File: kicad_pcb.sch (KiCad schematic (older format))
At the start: 162 parts, among them J1 USB_B_Mini, SW1 SW_Push, U1 ATmega32U4-AU, Y1 16Mhz

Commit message: further tracing applied
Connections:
- net COL0: now also U1.29 (PB5)
- net COL1: now also U1.30 (PB6)
- net COL10: now also U1.22 (PD5)
- net COL11: now also U1.21 (PD3)
- net COL12: now also U1.20 (PD2)
- net COL13: now also U1.19 (PD1)
- net COL14: now also U1.12 (PB7)
- net COL2: now also U1.41 (PF0)
- net COL3: now also U1.31 (PC6)
- net COL4: now also U1.32 (PC7)
- net COL5: now also U1.18 (PD0)
- net COL6: now also U1.1 (PE6)
- net COL7: now also U1.27 (PD7)
- net COL8: now also U1.28 (PB4)
- net COL9: now also U1.11 (PB3)
- net ROW0: now also U1.8 (PB0)
- net ROW1: now also U1.9 (PB1)
- net ROW2: now also U1.10 (PB2)
- net ROW3: now also U1.26 (PD6)
- net ROW4: now also U1.25 (PD4)
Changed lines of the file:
@@
 $EndDescr
-$Comp
-L MCU_Microchip_ATmega:ATmega32U4-AU U1
-U 1 1 5CCAF324
-P 8775 11800
-F 0 "U1" H 8775 9911 50  0000 C CNN
-F 1 "ATmega32U4-AU" H 8775 9820 50  0000 C CNN
-F 2 "Package_QFP:TQFP-44_10x10mm_P0.8mm" H 8775 11800 50  0001 C CIN
-F 3 "http://ww1.microchip.com/downloads/en/DeviceDoc/Atmel-7766-8-bit-AVR-ATmega16U4-32U4_Datasheet.pdf" H 8775 11800 50  0001 C CNN
-	1    8775 11800
-	1    0    0    -1
-$EndComp
 $Comp
 L Device:R_Small R4
@@
 Wire Wire Line
 	8675 10000 8675 9850
-Wire Wire Line
-	8875 10000 8775 10000
-Connection ~ 8675 10000
-Connection ~ 8775 10000
-Wire Wire Line
-	8775 10000 8675 10000
 $Comp
 L power:GND #PWR0103
@@
 $EndComp
 Wire Wire Line
-	8775 13600 8675 13600
-Connection ~ 8675 13600
-Wire Wire Line
-	8675 13600 8275 13600
-Wire Wire Line
 	10500 12400 10200 12400
-Wire Wire Line
-	10000 12400 9375 12400
 $Comp
 L Device:R_Small R2
@@
 	5000 5050 5000 6050
 Connection ~ 5000 5050
+Text GLabel 9475 12100 2    50   Input ~ 0
+ROW3
+Text GLabel 9475 10500 2    50   Input ~ 0
+ROW2
+Text GLabel 9475 10400 2    50   Input ~ 0
+ROW1
+Text GLabel 9475 10300 2    50   Input ~ 0
+ROW0
+Text GLabel 9475 11700 2    50   Input ~ 0
+COL12
+Text GLabel 9475 11600 2    50   Input ~ 0
+COL13
+Text GLabel 9475 12000 2    50   Input ~ 0
+COL10
+Text GLabel 9475 12200 2    50   Input ~ 0
+COL7
+Text GLabel 9475 11300 2    50   Input ~ 0
+COL4
+Text GLabel 9475 11500 2    50   Input ~ 0
+COL5
+Text GLabel 9475 11200 2    50   Input ~ 0
+COL3
+Text GLabel 9475 10800 2    50   Input ~ 0
+COL0
+Text GLabel 9475 12700 2    50   Input ~ 0
+COL2
+Text GLabel 9475 10900 2    50   Input ~ 0
+COL1
+Connection ~ 8675 13600
+Wire Wire Line
+	8675 13600 8275 13600
+Wire Wire Line
+	8775 13600 8675 13600
+Connection ~ 8775 10000
+Connection ~ 8675 10000
+Wire Wire Line
+	8775 10000 8675 10000
+Wire Wire Line
+	8875 10000 8775 10000
+Wire Wire Line
+	10000 12400 9375 12400
+$Comp
+L MCU_Microchip_ATmega:ATmega32U4-AU U1
+U 1 1 5CCAF324
+P 8775 11800
+F 0 "U1" H 8775 9911 50  0000 C CNN
+F 1 "ATmega32U4-AU" H 8775 9820 50  0000 C CNN
+F 2 "Package_QFP:TQFP-44_10x10mm_P0.8mm" H 8775 11800 50  0001 C CIN
+F 3 "http://ww1.microchip.com/downloads/en/DeviceDoc/Atmel-7766-8-bit-AVR-ATmega16U4-32U4_Datasheet.pdf" H 8775 11800 50  0001 C CNN
+	1    8775 11800
+	1    0    0    -1
+$EndComp
+Text GLabel 9475 11000 2    50   Input ~ 0
+COL14
+Wire Wire Line
+	9375 10400 9475 10400
+Wire Wire Line
+	9475 10300 9375 10300
+Wire Wire Line
+	9375 10500 9475 10500
+Wire Wire Line
+	9475 10600 9375 10600
+Wire Wire Line
+	9375 10700 9475 10700
+Wire Wire Line
+	9475 10800 9375 10800
+Wire Wire Line
+	9375 10900 9475 10900
+Wire Wire Line
+	9475 11000 9375 11000
+Wire Wire Line
+	9375 11200 9475 11200
+Wire Wire Line
+	9475 11300 9375 11300
+Wire Wire Line
+	9375 11500 9475 11500
+Wire Wire Line
+	9375 11700 9475 11700
+Wire Wire Line
+	9375 11900 9475 11900
+Wire Wire Line
+	9375 12000 9475 12000
+Wire Wire Line
+	9375 12200 9475 12200
+Wire Wire Line
+	9375 12500 9475 12500
+Wire Wire Line
+	9475 12700 9375 12700
+Wire Wire Line
+	9475 11800 9375 11800
+Wire Wire Line
+	9475 12100 9375 12100
+Wire Wire Line
+	9475 11600 9375 11600
+Text GLabel 9475 12500 2    50   Input ~ 0
+COL6
+Text GLabel 9475 11900 2    50   Input ~ 0
+ROW4
+Text GLabel 9475 10700 2    50   Input ~ 0
+COL8
+Text GLabel 9475 11800 2    50   Input ~ 0
+COL11
+Text GLabel 9475 10600 2    50   Input ~ 0
+COL9
 $EndSCHEMATC

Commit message: first draft of the v2 PCB completed
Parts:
- MX59: value MX-1U -> SLASH
- MX60: value MX-1U -> R SHIFT
- MX61: value MX-1U -> FN
- MX62: value MX-1U -> CTRL
- MX63: value MX-1U -> WIN
- MX64: value MX-1U -> ALT
- MX65: value MX-1U -> LEFT SPACE; footprint MX_Alps_Hybrid:MXOnly-2.25U-NoLED -> MX_Alps_Hybrid:MXOnly-2.25U-ReversedStabilizers-NoLED
- MX68: value MX-1U -> CENTER
- MX70: value MX-1U -> RIGHT SPACE; footprint MX_Alps_Hybrid:MXOnly-2U-NoLED -> MX_Alps_Hybrid:MXOnly-2U-ReversedStabilizers-NoLED
- MX71: value MX-1U -> LEFT
- MX72: value MX-1U -> DOWN
- MX73: value MX-1U -> UP
- MX74: value MX-1U -> RIGHT
- MX75: value MX-1U -> Fn
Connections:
- net COL0: now also U1.1 (PE6); no longer U1.29 (PB5)
- net COL1: now also U1.41 (PF0); no longer U1.30 (PB6)
- net COL10: now also U1.25 (PD4); no longer U1.22 (PD5)
- net COL11: now also U1.22 (PD5); no longer U1.21 (PD3)
- net COL12: now also U1.21 (PD3); no longer U1.20 (PD2)
- net COL13: now also U1.20 (PD2); no longer U1.19 (PD1)
- net COL14: now also U1.19 (PD1); no longer U1.12 (PB7)
- net COL2: now also U1.40 (PF1); no longer U1.41 (PF0)
- net COL3: now also U1.39 (PF4); no longer U1.31 (PC6)
- net COL4: now also U1.37 (PF6); no longer U1.32 (PC7)
- net COL5: now also U1.36 (PF7); no longer U1.18 (PD0)
- net COL6: now also U1.38 (PF5); no longer U1.1 (PE6)
- net COL7: now also U1.31 (PC6); no longer U1.27 (PD7)
- net COL9: now also U1.26 (PD6); no longer U1.11 (PB3)
- net ROW1: now also U1.18 (PD0); no longer U1.9 (PB1)
- net ROW2: now also U1.29 (PB5); no longer U1.10 (PB2)
- net ROW3: now also U1.12 (PB7); no longer U1.26 (PD6)
- net ROW4: now also U1.30 (PB6); no longer U1.25 (PD4)
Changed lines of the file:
@@
 P 21075 6075
 F 0 "MX75" H 21161 6292 60  0000 C CNN
-F 1 "MX-1U" H 21161 6218 20  0000 C CNN
+F 1 "Fn" H 21161 6218 20  0000 C CNN
 F 2 "MX_Alps_Hybrid:MXOnly-1U-NoLED" H 21050 6050 60  0001 C CNN
 F 3 "" H 21050 6050 60  0001 C CNN
@@
 P 19825 6075
 F 0 "MX74" H 19911 6292 60  0000 C CNN
-F 1 "MX-1U" H 19911 6218 20  0000 C CNN
+F 1 "RIGHT" H 19911 6218 20  0000 C CNN
 F 2 "MX_Alps_Hybrid:MXOnly-1U-NoLED" H 19800 6050 60  0001 C CNN
 F 3 "" H 19800 6050 60  0001 C CNN
@@
 P 18575 6075
 F 0 "MX73" H 18661 6292 60  0000 C CNN
-F 1 "MX-1U" H 18661 6218 20  0000 C CNN
+F 1 "UP" H 18661 6218 20  0000 C CNN
 F 2 "MX_Alps_Hybrid:MXOnly-1U-NoLED" H 18550 6050 60  0001 C CNN
 F 3 "" H 18550 6050 60  0001 C CNN
@@
 P 17325 6075
 F 0 "MX72" H 17411 6292 60  0000 C CNN
-F 1 "MX-1U" H 17411 6218 20  0000 C CNN
+F 1 "DOWN" H 17411 6218 20  0000 C CNN
 F 2 "MX_Alps_Hybrid:MXOnly-1U-NoLED" H 17300 6050 60  0001 C CNN
 F 3 "" H 17300 6050 60  0001 C CNN
@@
 P 16075 6075
 F 0 "MX71" H 16161 6292 60  0000 C CNN
-F 1 "MX-1U" H 16161 6218 20  0000 C CNN
+F 1 "LEFT" H 16161 6218 20  0000 C CNN
 F 2 "MX_Alps_Hybrid:MXOnly-1U-NoLED" H 16050 6050 60  0001 C CNN
 F 3 "" H 16050 6050 60  0001 C CNN
@@
 P 14825 6075
 F 0 "MX70" H 14911 6292 60  0000 C CNN
-F 1 "MX-1U" H 14911 6218 20  0000 C CNN
-F 2 "MX_Alps_Hybrid:MXOnly-2U-NoLED" H 14800 6050 60  0001 C CNN
+F 1 "RIGHT SPACE" H 14911 6218 20  0000 C CNN
+F 2 "MX_Alps_Hybrid:MXOnly-2U-ReversedStabilizers-NoLED" H 14800 6050 60  0001 C CNN
 F 3 "" H 14800 6050 60  0001 C CNN
 	1    14825 6075
@@
 P 12325 6075
 F 0 "MX68" H 12411 6292 60  0000 C CNN
-F 1 "MX-1U" H 12411 6218 20  0000 C CNN
+F 1 "CENTER" H 12411 6218 20  0000 C CNN
 F 2 "MX_Alps_Hybrid:MXOnly-1U-NoLED" H 12300 6050 60  0001 C CNN
 F 3 "" H 12300 6050 60  0001 C CNN
@@
 P 8575 6075
 F 0 "MX65" H 8661 6292 60  0000 C CNN
-F 1 "MX-1U" H 8661 6218 20  0000 C CNN
-F 2 "MX_Alps_Hybrid:MXOnly-2.25U-NoLED" H 8550 6050 60  0001 C CNN
+F 1 "LEFT SPACE" H 8661 6218 20  0000 C CNN
+F 2 "MX_Alps_Hybrid:MXOnly-2.25U-ReversedStabilizers-NoLED" H 8550 6050 60  0001 C CNN
 F 3 "" H 8550 6050 60  0001 C CNN
 	1    8575 6075
@@
 P 7325 6075
 F 0 "MX64" H 7411 6292 60  0000 C CNN
-F 1 "MX-1U" H 7411 6218 20  0000 C CNN
+F 1 "ALT" H 7411 6218 20  0000 C CNN
 F 2 "MX_Alps_Hybrid:MXOnly-1.25U-NoLED" H 7300 6050 60  0001 C CNN
 F 3 "" H 7300 6050 60  0001 C CNN
@@
 P 4825 6075
 F 0 "MX62" H 4911 6292 60  0000 C CNN
-F 1 "MX-1U" H 4911 6218 20  0000 C CNN
+F 1 "CTRL" H 4911 6218 20  0000 C CNN
 F 2 "MX_Alps_Hybrid:MXOnly-1.25U-NoLED" H 4800 6050 60  0001 C CNN
 F 3 "" H 4800 6050 60  0001 C CNN
@@
 P 3575 6075
 F 0 "MX61" H 3661 6292 60  0000 C CNN
-F 1 "MX-1U" H 3661 6218 20  0000 C CNN
+F 1 "FN" H 3661 6218 20  0000 C CNN
 F 2 "MX_Alps_Hybrid:MXOnly-1U-NoLED" H 3550 6050 60  0001 C CNN
 F 3 "" H 3550 6050 60  0001 C CNN
@@
 P 6075 6075
 F 0 "MX63" H 6161 6292 60  0000 C CNN
-F 1 "MX-1U" H 6161 6218 20  0000 C CNN
+F 1 "WIN" H 6161 6218 20  0000 C CNN
 F 2 "MX_Alps_Hybrid:MXOnly-1.25U-NoLED" H 6050 6050 60  0001 C CNN
 F 3 "" H 6050 6050 60  0001 C CNN
@@
 P 21075 5075
 F 0 "MX60" H 21161 5292 60  0000 C CNN
-F 1 "MX-1U" H 21161 5218 20  0000 C CNN
+F 1 "R SHIFT" H 21161 5218 20  0000 C CNN
 F 2 "MX_Alps_Hybrid:MXOnly-1U-NoLED" H 21050 5050 60  0001 C CNN
 F 3 "" H 21050 5050 60  0001 C CNN
@@
 P 19825 5075
 F 0 "MX59" H 19911 5292 60  0000 C CNN
-F 1 "MX-1U" H 19911 5218 20  0000 C CNN
+F 1 "SLASH" H 19911 5218 20  0000 C CNN
 F 2 "MX_Alps_Hybrid:MXOnly-1U-NoLED" H 19800 5050 60  0001 C CNN
 F 3 "" H 19800 5050 60  0001 C CNN
@@
 	5000 5050 5000 6050
 Connection ~ 5000 5050
-Text GLabel 9475 12100 2    50   Input ~ 0
-ROW3
-Text GLabel 9475 10500 2    50   Input ~ 0
+Text GLabel 9475 10800 2    50   Input ~ 0
 ROW2
-Text GLabel 9475 10400 2    50   Input ~ 0
-ROW1
 Text GLabel 9475 10300 2    50   Input ~ 0
 ROW0
+Text GLabel 9475 11800 2    50   Input ~ 0
+COL12
 Text GLabel 9475 11700 2    50   Input ~ 0
-COL12
-Text GLabel 9475 11600 2    50   Input ~ 0
 COL13
-Text GLabel 9475 12000 2    50   Input ~ 0
+Text GLabel 9475 11900 2    50   Input ~ 0
 COL10
-Text GLabel 9475 12200 2    50   Input ~ 0
-COL7
-Text GLabel 9475 11300 2    50   Input ~ 0
+Text GLabel 9475 13100 2    50   Input ~ 0
 COL4
-Text GLabel 9475 11500 2    50   Input ~ 0
+Text GLabel 9475 13200 2    50   Input ~ 0
 COL5
-Text GLabel 9475 11200 2    50   Input ~ 0
+Text GLabel 9475 12900 2    50   Input ~ 0
 COL3
-Text GLabel 9475 10800 2    50   Input ~ 0
+Text GLabel 9475 12500 2    50   Input ~ 0
 COL0
+Text GLabel 9475 12800 2    50   Input ~ 0
+COL2
 Text GLabel 9475 12700 2    50   Input ~ 0
-COL2
-Text GLabel 9475 10900 2    50   Input ~ 0
 COL1
 Connection ~ 8675 13600
@@
 	1    0    0    -1
 $EndComp
-Text GLabel 9475 11000 2    50   Input ~ 0
+Text GLabel 9475 11600 2    50   Input ~ 0
 COL14
 Wire Wire Line
@@
 Wire Wire Line
 	9475 11600 9375 11600
-Text GLabel 9475 12500 2    50   Input ~ 0
+Text GLabel 9475 13000 2    50   Input ~ 0
 COL6
-Text GLabel 9475 11900 2    50   Input ~ 0
-ROW4
 Text GLabel 9475 10700 2    50   Input ~ 0
 COL8
-Text GLabel 9475 11800 2    50   Input ~ 0
+Wire Wire Line
+	9475 12800 9375 12800
+Wire Wire Line
+	9375 12900 9475 12900
+Wire Wire Line
+	9475 13000 9375 13000
+Wire Wire Line
+	9375 13100 9475 13100
+Wire Wire Line
+	9475 13200 9375 13200
+Text GLabel 9475 10900 2    50   Input ~ 0
+ROW4
+Text GLabel 9475 11000 2    50   Input ~ 0
+ROW3
+Text GLabel 9475 12100 2    50   Input ~ 0
+COL9
+Text GLabel 9475 12000 2    50   Input ~ 0
 COL11
-Text GLabel 9475 10600 2    50   Input ~ 0
-COL9
+Text GLabel 9475 11200 2    50   Input ~ 0
+COL7
+Text GLabel 9475 11500 2    50   Input ~ 0
+ROW1
 $EndSCHEMATC

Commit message: ready to export
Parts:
- C1, C2, C3, C4, C5, C6: footprint Capacitor_SMD:C_0201_0603Metric -> Capacitor_SMD:C_0805_2012Metric
- R2, R3: footprint Resistor_SMD:R_0603_1608Metric -> Resistor_SMD:R_0805_2012Metric
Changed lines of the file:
@@
 F 0 "R2" V 6879 11300 50  0000 C CNN
 F 1 "22" V 6970 11300 50  0000 C CNN
-F 2 "Resistor_SMD:R_0603_1608Metric" H 7075 11300 50  0001 C CNN
+F 2 "Resistor_SMD:R_0805_2012Metric" H 7075 11300 50  0001 C CNN
 F 3 "~" H 7075 11300 50  0001 C CNN
 	1    7075 11300
@@
 F 0 "R3" V 6604 11400 50  0000 C CNN
 F 1 "22" V 6695 11400 50  0000 C CNN
-F 2 "Resistor_SMD:R_0603_1608Metric" H 6800 11400 50  0001 C CNN
+F 2 "Resistor_SMD:R_0805_2012Metric" H 6800 11400 50  0001 C CNN
 F 3 "~" H 6800 11400 50  0001 C CNN
 	1    6800 11400
@@
 F 0 "C3" H 7667 11746 50  0000 L CNN
 F 1 "1uF" H 7667 11655 50  0000 L CNN
-F 2 "Capacitor_SMD:C_0201_0603Metric" H 7575 11700 50  0001 C CNN
+F 2 "Capacitor_SMD:C_0805_2012Metric" H 7575 11700 50  0001 C CNN
 F 3 "~" H 7575 11700 50  0001 C CNN
 	1    7575 11700
@@
 F 0 "C5" H 6842 12646 50  0000 L CNN
 F 1 "0.1uF" H 6842 12555 50  0000 L CNN
-F 2 "Capacitor_SMD:C_0201_0603Metric" H 6750 12600 50  0001 C CNN
+F 2 "Capacitor_SMD:C_0805_2012Metric" H 6750 12600 50  0001 C CNN
 F 3 "~" H 6750 12600 50  0001 C CNN
 	1    6750 12600
@@
 F 0 "C6" H 7342 12646 50  0000 L CNN
 F 1 "0.1uF" H 7342 12555 50  0000 L CNN
-F 2 "Capacitor_SMD:C_0201_0603Metric" H 7250 12600 50  0001 C CNN
+F 2 "Capacitor_SMD:C_0805_2012Metric" H 7250 12600 50  0001 C CNN
 F 3 "~" H 7250 12600 50  0001 C CNN
 	1    7250 12600
@@
 F 0 "C4" H 6342 12646 50  0000 L CNN
 F 1 "0.1uF" H 6342 12555 50  0000 L CNN
-F 2 "Capacitor_SMD:C_0201_0603Metric" H 6250 12600 50  0001 C CNN
+F 2 "Capacitor_SMD:C_0805_2012Metric" H 6250 12600 50  0001 C CNN
 F 3 "~" H 6250 12600 50  0001 C CNN
 	1    6250 12600
@@
 F 0 "C1" V 6871 10425 50  0000 C CNN
 F 1 "22pF" V 6962 10425 50  0000 C CNN
-F 2 "Capacitor_SMD:C_0201_0603Metric" H 7100 10425 50  0001 C CNN
+F 2 "Capacitor_SMD:C_0805_2012Metric" H 7100 10425 50  0001 C CNN
 F 3 "~" H 7100 10425 50  0001 C CNN
 	1    7100 10425
@@
 F 0 "C2" V 6871 10775 50  0000 C CNN
 F 1 "22pF" V 6962 10775 50  0000 C CNN
-F 2 "Capacitor_SMD:C_0201_0603Metric" H 7100 10775 50  0001 C CNN
+F 2 "Capacitor_SMD:C_0805_2012Metric" H 7100 10775 50  0001 C CNN
 F 3 "~" H 7100 10775 50  0001 C CNN
 	1    7100 10775

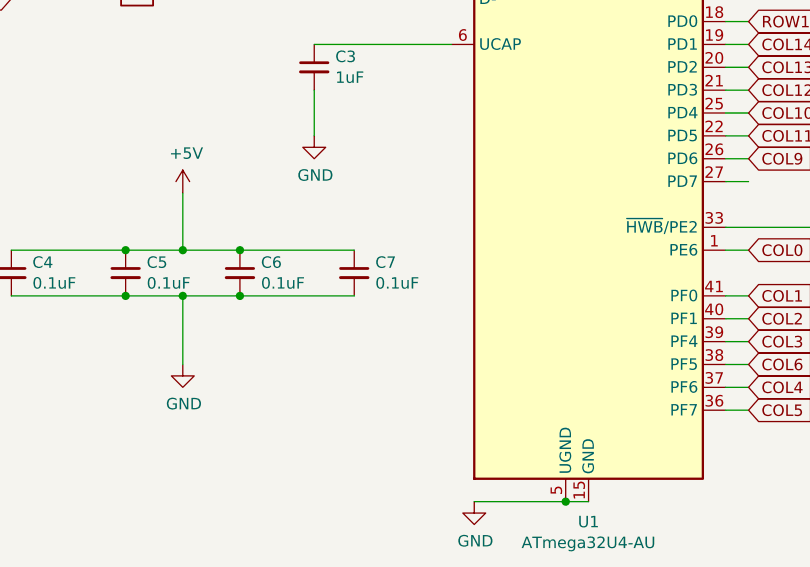
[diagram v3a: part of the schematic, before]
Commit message: ammended some incorrect footprints
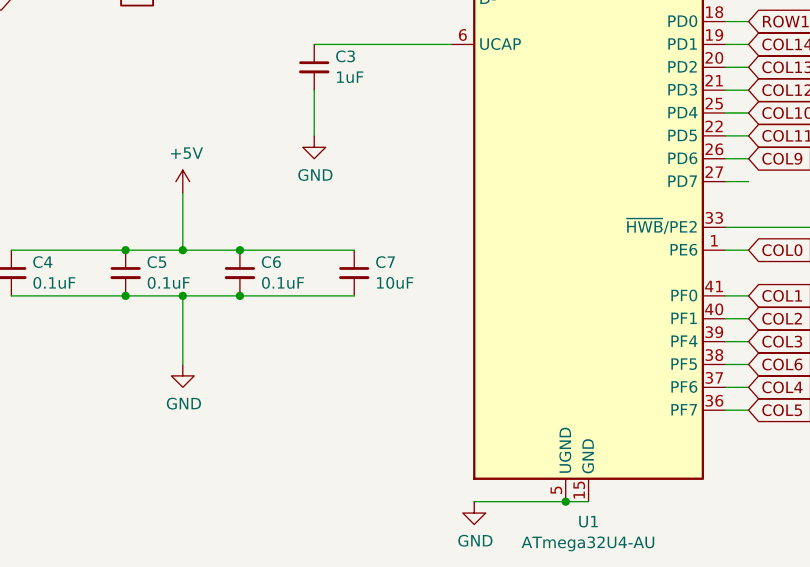
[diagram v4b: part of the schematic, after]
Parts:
- C7: value 0.1uF -> 10uF
- F1: footprint Fuse:Fuse_0805_2012Metric -> Fuse:Fuse_1206_3216Metric
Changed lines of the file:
@@
 P 7750 12600
 F 0 "C7" H 7842 12646 50  0000 L CNN
-F 1 "0.1uF" H 7842 12555 50  0000 L CNN
+F 1 "10uF" H 7842 12555 50  0000 L CNN
 F 2 "Diode_SMD:D_0805_2012Metric" H 7750 12600 50  0001 C CNN
 F 3 "~" H 7750 12600 50  0001 C CNN
@@
 F 0 "F1" V 4420 10000 50  0000 C CNN
 F 1 "500mA" V 4511 10000 50  0000 C CNN
-F 2 "Fuse:Fuse_0805_2012Metric" H 4675 9800 50  0001 L CNN
+F 2 "Fuse:Fuse_1206_3216Metric" H 4675 9800 50  0001 L CNN
 F 3 "~" H 4625 10000 50  0001 C CNN
 	1    4625 10000
